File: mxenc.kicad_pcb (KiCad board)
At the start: 8 copper layers, 65 x 32 mm, 273 parts, among them J1 USB_C_Receptacle, J2 Bus_PCI_Express_Mini, J3 Micro_SD_Card, J4 Conn_01x06, J5 Conn_01x02, J6 Conn_01x06, J7 DF40HC(3.5)-60DS, J8 Conn_01x06 DNP, J9 DF40HC(3.5)-60DS, Q2 AON7405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

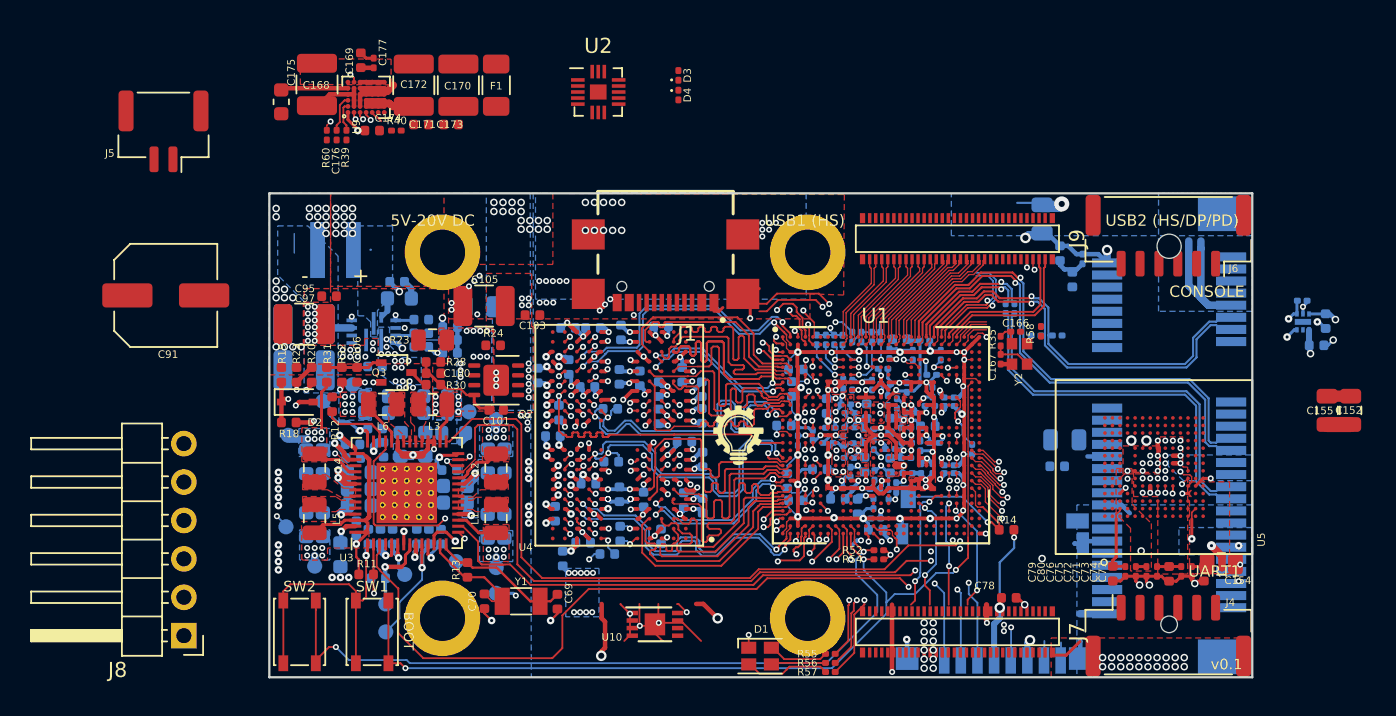
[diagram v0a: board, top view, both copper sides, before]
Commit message: rough layout, routing for emmc and csi, dsi, pcie
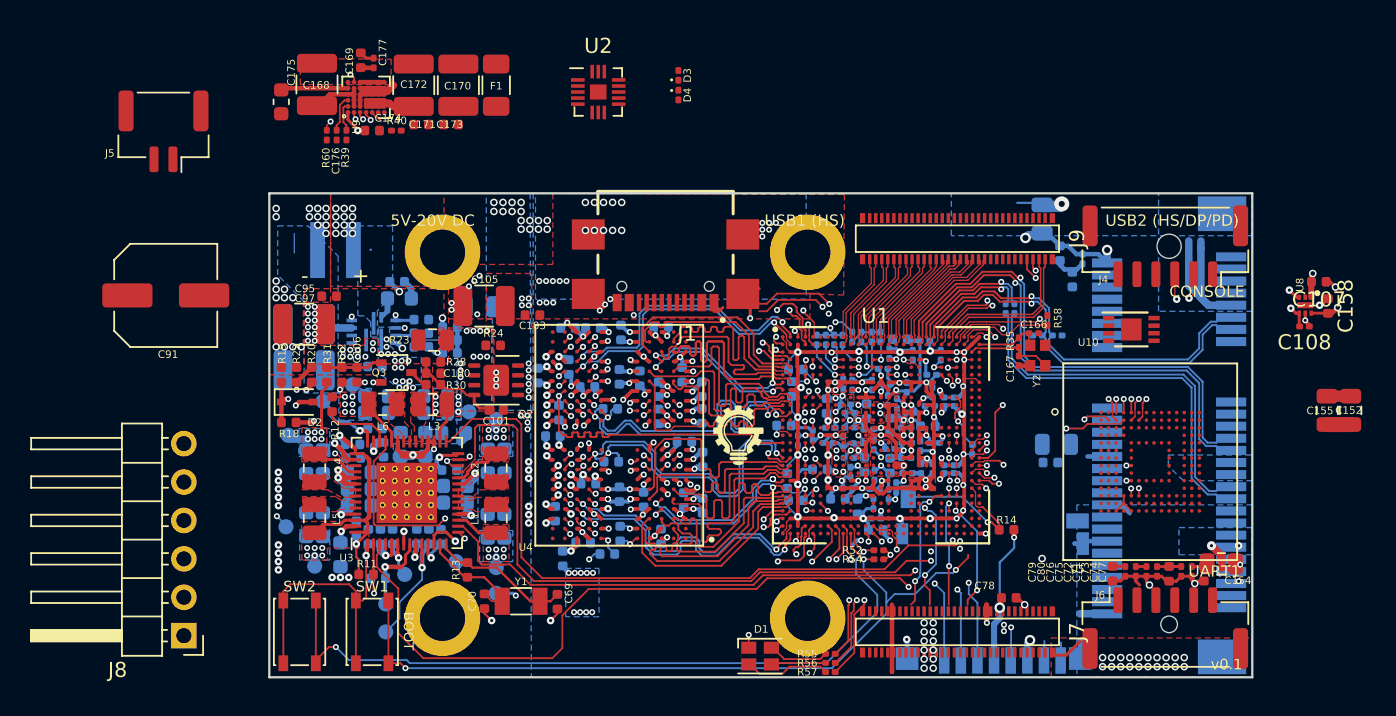
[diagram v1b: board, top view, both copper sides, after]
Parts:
- C107, C108, C158, U8: moved to F.Cu
- moved U10 37.0 mm to (164.0, 103.0)
- moved J6 26.0 mm to (166.2, 122.8), turned to 0 degrees
- moved J4 25.8 mm to (166.2, 97.5), turned to 180 degrees
- moved C107 4.20 mm to (176.4, 99.8)
- moved C108 1.71 mm to (175.4, 102.8)
- moved C166 1.20 mm to (157.6, 103.2)
- moved R35 1.20 mm to (156.6, 103.9)
- moved C167 1.20 mm to (156.6, 105.1)
- moved Y2 1.20 mm to (157.8, 104.7)
- moved U8 1.11 mm to (175.5, 101.4), turned to 270 degrees
- moved C158 1.01 mm to (177.0, 101.5), turned to 270 degrees
- moved R58 0.84 mm to (158.4, 102.4), turned to 90 degrees
- moved C153 0.63 mm to (159.1, 110.6)
- moved C157 0.51 mm to (158.7, 111.8)
- moved U5 0.43 mm to (165.2, 111.8), turned to 0 degrees
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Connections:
- net Net-(C79-Pad1) renamed /SD/MMC/EMMC_VDDI
- J3 pad 9: (no net) -> GND
- U1 pad AC6: /UART2_RX -> (no net)
- U1 pad AF7: /UART2_RTS_B -> (no net)
- U1 pad AG6: /UART2_TX -> (no net)
- U1 pad AG7: /UART2_CTS_B -> (no net)
- U1 pad E15: (no net) -> /UART2_TX
- U1 pad F15: (no net) -> /UART2_RX
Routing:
- net /I2C3_SDA: track 49.8 -> 11.4 mm, vias 4 -> 3
- net /I2C3_SCL: track 47.5 -> 12.2 mm, vias 5 -> 3
- net /UART2_RTS_B: track 23.8 -> 0.00 mm, vias 2 -> 0
- net /LD1_~INT: track 24.2 -> 1.03 mm
- net /UART2_CTS_B: track 19.1 -> 0.00 mm, vias 2 -> 0
- net (no net): track 33.1 -> 50.3 mm, vias 58 -> 56
- net /BTN0: track 64.0 -> 52.5 mm
- net GND: track 272.1 -> 262.2 mm, vias 227 -> 209
- net /SD/MMC/EMMC_DAT4: track 10.4 -> 20.2 mm
- net /SD/MMC/EMMC_DAT0: track 11.8 -> 20.3 mm, vias 1 -> 2
- net /SD/MMC/EMMC_DAT3: track 11.8 -> 20.1 mm, vias 1 -> 2
- net /SD/MMC/EMMC_DAT2: track 12.1 -> 20.0 mm, vias 3 -> 2
- net /SD/MMC/EMMC_DAT6: track 12.6 -> 20.1 mm, vias 1 -> 2
- net /SD/MMC/EMMC_DAT1: track 12.8 -> 20.2 mm, vias 1 -> 2
- net /SD/MMC/EMMC_DAT5: track 12.8 -> 19.9 mm, vias 3 -> 2
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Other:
- net class CSI/DSI: trace_width 0.127 -> 0.121666
- net class Default: trace_width 0.12192 -> 0.121666
- net class PCIE: trace_width 0.127 -> 0.121666
- net class USB: trace_width 0.127 -> 0.121666

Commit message: More new layout, buttons, and routing
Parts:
- C107, C108, C158, U8: moved to B.Cu
- C157: moved to F.Cu
- SW1, SW2: footprint Button_Switch_SMD:SW_SPST_PTS810 -> mxenc:SW_SPST_EVQP7C
- moved SW1 62.2 mm to (170.4, 97.2), turned to 90 degrees
- moved SW2 60.6 mm to (163.0, 95.6), turned to 180 degrees
- moved J4 42.7 mm to (132.2, 123.2), turned to 0 degrees
- moved R54 30.5 mm to (167.6, 95.5), turned to 270 degrees
- moved R52 29.5 mm to (166.8, 95.5), turned to 270 degrees
- moved C152 22.3 mm to (158.6, 118.4)
- moved C158 21.6 mm to (157.7, 111.1), turned to 180 degrees
- moved C108 21.5 mm to (156.3, 112.7), turned to 270 degrees
- moved U8 21.0 mm to (157.7, 112.6), turned to 180 degrees
- moved C107 20.8 mm to (159.2, 111.7), turned to 270 degrees
- moved C155 19.6 mm to (158.6, 115.3), turned to 270 degrees
- moved J5 14.3 mm to (112.1, 97.5)
- moved U2 10.9 mm to (139.7, 87.8)
- moved C157 8.04 mm to (161.9, 119.2), turned to 90 degrees
- moved U10 5.76 mm to (169.8, 102.7), turned to 270 degrees
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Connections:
- J7 pad MP: (no net) -> GND
- J9 pad 51: (no net) -> JTAG_MOD
- J9 pad 52: (no net) -> JTAG_TRST_B
- J9 pad 53: (no net) -> JTAG_TDO
- J9 pad 54: (no net) -> JTAG_TDI
- J9 pad 55: (no net) -> JTAG_TMS
- J9 pad 56: (no net) -> JTAG_TCK
- J9 pad MP: (no net) -> GND
- R52 pad 2: /BTN1 -> GPIO3[5]
- R54 pad 2: /BTN0 -> GPIO3[12]
- SW1 pad 1: /BTN0 -> GPIO3[12]
- SW1 pad 2: NVCC_3V3 -> NVCC_1V8
- SW2 pad 1: /BTN1 -> GPIO3[5]
- SW2 pad 2: NVCC_3V3 -> NVCC_1V8
- U1 pad AF10: /BTN1 -> (no net)
- U1 pad AG10: /BTN0 -> (no net)
- U1 pad C27: (no net) -> JTAG_TRST_B
- U1 pad D27: (no net) -> JTAG_MOD
- U1 pad E26: (no net) -> JTAG_TDO
- U1 pad E27: (no net) -> JTAG_TDI
- U1 pad F26: (no net) -> JTAG_TCK
- U1 pad F27: (no net) -> JTAG_TMS
- U1 pad G26: /BTN0 -> GPIO3[12]
- U1 pad K26: (no net) -> GPIO3[12]
- U1 pad K27: (no net) -> GPIO3[5]
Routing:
- net /BTN0: track 52.5 -> 0.00 mm, vias 3 -> 0
- net /BTN1: track 51.2 -> 0.00 mm, vias 2 -> 0
- net GPIO3[12]: track 0.00 -> 31.2 mm
- net /UART2_TX: track 24.7 -> 0.00 mm, vias 2 -> 0
- net /UART2_RX: track 24.1 -> 0.00 mm, vias 2 -> 0
- net GPIO3[5]: track 0.00 -> 22.7 mm
- net NVCC_3V3: track 62.8 -> 42.3 mm, vias 18 -> 16
- net GND: track 262.2 -> 248.1 mm, vias 209 -> 196
- net JTAG_TCK: track 0.00 -> 12.5 mm, vias 0 -> 2
- net JTAG_TMS: track 0.00 -> 11.8 mm, vias 0 -> 2
- net JTAG_TDO: track 0.00 -> 10.9 mm, vias 0 -> 2
- net JTAG_TDI: track 0.00 -> 10.1 mm, vias 0 -> 2
- net /I2C2_SCL: track 12.1 -> 2.25 mm, vias 2 -> 1
- net (no net): track 50.3 -> 40.5 mm, vias 56 -> 40
- net /I2C2_SDA: track 10.7 -> 1.66 mm, vias 2 -> 1
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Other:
- net class Default: via_dia 0.5 -> 0.4
- board text removed: "USB2 (HS/DP/PD)"
